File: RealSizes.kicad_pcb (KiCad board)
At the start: 2 copper layers, 104 parts

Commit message: Plots
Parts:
- removed the REF** at (143.3, 39.9)
- removed the REF** at (26.2, 20.1)
- removed the REF** at (228.6, 41.9)
- removed the REF** at (103.6, 127.0)
- removed the REF** at (139.2, 191.3)
- removed the REF** at (103.6, 114.3)
- added 01005_0402M: C_01005_0402Metric, Capacitor_SMD:C_01005_0402Metric, F.Cu at (264.5, 14.5)
- 5x1206: renamed from REF**; value R_Array_Convex_5x1206 -> 5x1206
- SMA-SMB: renamed from REF**; value D_SMA-SMB_Universal_Handsoldering -> SMA-SMB_Universal_Handsoldering
- TO-252-2 DPAK: renamed from REF**
- TO-263-2 DDPAK: renamed from REF**
- TO-5-8, TO-78-8, TO-99-8 : renamed from REF**
- moved 5x1206 239.6 mm to (262.5, 61.5), turned to 90 degrees
- moved 0402_1005M 238.5 mm to (264.5, 18.0)
- moved 0201_0603M 238.5 mm to (264.5, 16.0)
- moved 0805_2012M 238.0 mm to (264.0, 22.5)
- moved 2010_5025M 238.0 mm to (263.0, 38.5)
- moved 0603_1608M 237.9 mm to (264.0, 20.0)
- moved 2512_6332M 237.8 mm to (262.5, 43.0)
- moved 1210_3225M 237.8 mm to (263.5, 29.5)
- moved 2816_7142M 237.7 mm to (262.0, 48.5)
- moved 1206_3216M 237.6 mm to (263.5, 25.5)
- moved 1812_4532M 237.6 mm to (263.0, 34.0)
- moved 4020_10251M 236.8 mm to (260.5, 55.0)
- moved DSUB-9_P2.77x2.84mm 179.0 mm to (24.7, 114.7)
- moved DSUB-15-HD_P2.29x1.98mm 178.1 mm to (26.0, 131.2)
- moved DSUB-15_P2.77x2.84mm 173.4 mm to (24.5, 149.8)
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- renumbered REF** to 0201_0603M, REF** to 0402_1005M, REF** to 0603_1608M, REF** to 0805_2012M, REF** to 1206_3216M, REF** to 1210_3225M, REF** to 1812_4532M, REF** to 2010_5025M, REF** to 2512_6332M, REF** to 2816_7142M, REF** to 4020_10251M, REF** to BGA-25_6.35x6.35mm_5x5_P1.27mm, REF** to CPGA196, REF** to CSG324, REF** to DFN-6_1.3x1.2mm_P0.4mm, REF** to DFN-8_2x2mm_P0.5mm, REF** to DFN1006-3, REF** to DIP-14_W7.62mm_Socket, REF** to DIP-8_W7.62mm_Socket, REF** to DSUB-15-HD_P2.29x1.98mm, REF** to DSUB-15_P2.77x2.84mm, REF** to DSUB-25_P2.77x2.84mm, REF** to DSUB-37_P2.77x2.84mm, REF** to DSUB-9_P2.77x2.84mm, REF** to LED_D10.0mm, REF** to LED_D3.0mm, REF** to LED_D4.0mm, REF** to LED_D5.0mm, REF** to LED_D8.0mm, REF** to MSOP-16_3x4.039mm_P0.5mm, REF** to MSOP-8_3x3mm_P0.65mm, REF** to MiniMELF, REF** to QFN-16-1EP_5x5mm_P0.8mm_EP2.7x2.7mm, REF** to SC-59, REF** to SC-70-8, REF** to SC-82AA, REF** to SO-8, REF** to SOD-123, REF** to SOD-323, REF** to SOD-523, REF** to SOD-882, REF** to SOIC-16_3.9x9.9mm_P1.27mm, REF** to SOT-223, REF** to SOT-223-5, REF** to SOT-223-6, REF** to SOT-223-8, REF** to SOT-23, REF** to SOT-23-5, REF** to SOT-323_SC-70, REF** to SOT-353_SC-70-5, REF** to SOT-523, REF** to SOT-89-3, REF** to TO-220-3, REF** to TO-220-3_Vertical, REF** to TO-220-5_P3.4x3.7mm_StaggerEven_Lead3.8mm, REF** to TO-220-5_P3.4x3.8mm_StaggerEven_Lead7.13mm, REF** to TO-247-3, REF** to TO-263-5, REF** to TO-268-2, REF** to TO-277A, REF** to TO-3, REF** to TO-92, REF** to TO-92Flat, REF** to TO-92L_Inline, REF** to TP1.0x1.0, REF** to TP1.0x1.0_Drl_0.5, REF** to TP1.5x1.5, REF** to TP1.5x1.5_Drl_0.7, REF** to TP2.0x2.0_Drl_1.0, REF** to TP2x2, REF** to TP3.0x3.0_Drl_1.5, REF** to TP3x3, REF** to TPD1.0mm, REF** to TPD1.0mm_Drl_0.5mm, REF** to TPD1.5mm, REF** to TPD1.5mm_Drl_0.7mm, REF** to TPD2.0mm, REF** to TPD2.0mm_PTH, REF** to TPD3.0mm, REF** to TPD3.0mm_PTH, REF** to TSOT-23, REF** to TSOT-23-5, REF** to TSOT-23-6, REF** to TSOT-23-8, REF** to TSSOP-16_4.4x3.6mm_P0.4mm, REF** to TSSOP-8_3x3mm_P0.65mm, REF** to WSON6_1.5x1.5mm_P0.5mm
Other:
- board text removed: "DDPAK"
- board text removed: "DPAK"

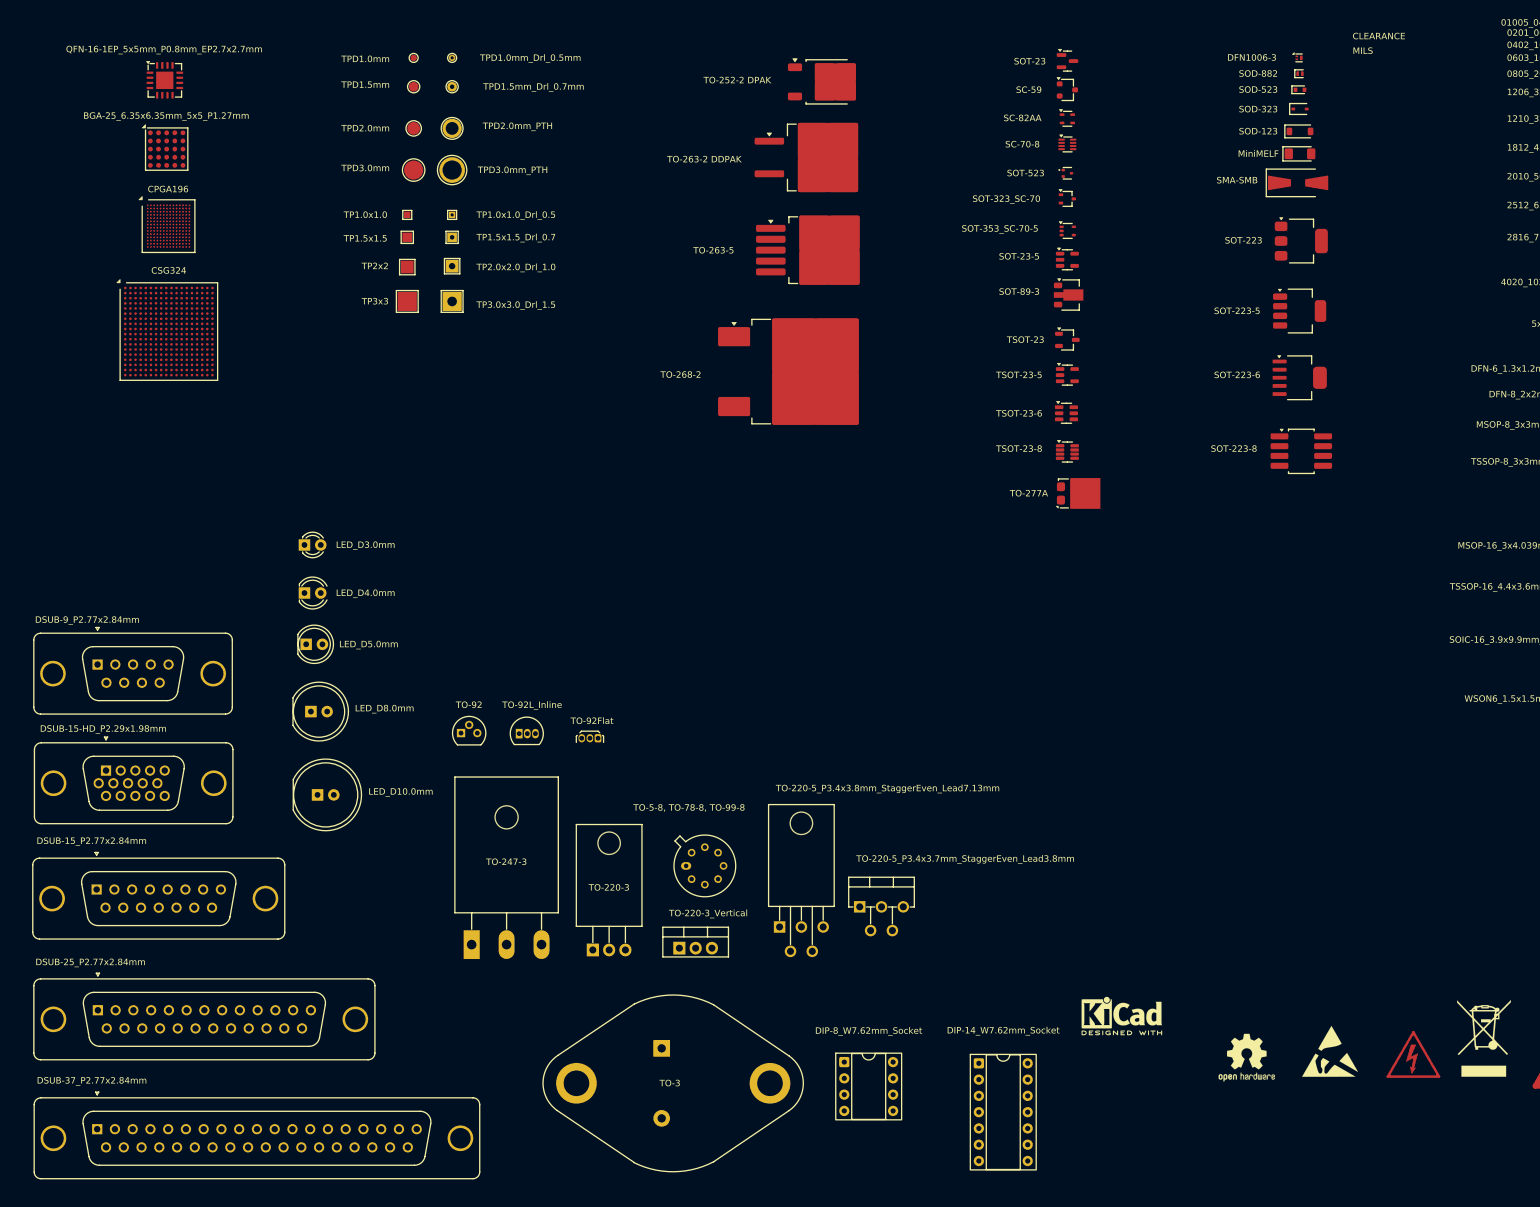
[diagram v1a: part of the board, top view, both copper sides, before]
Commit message: added diodes types
Need to ad diff, traces tracks c;learence
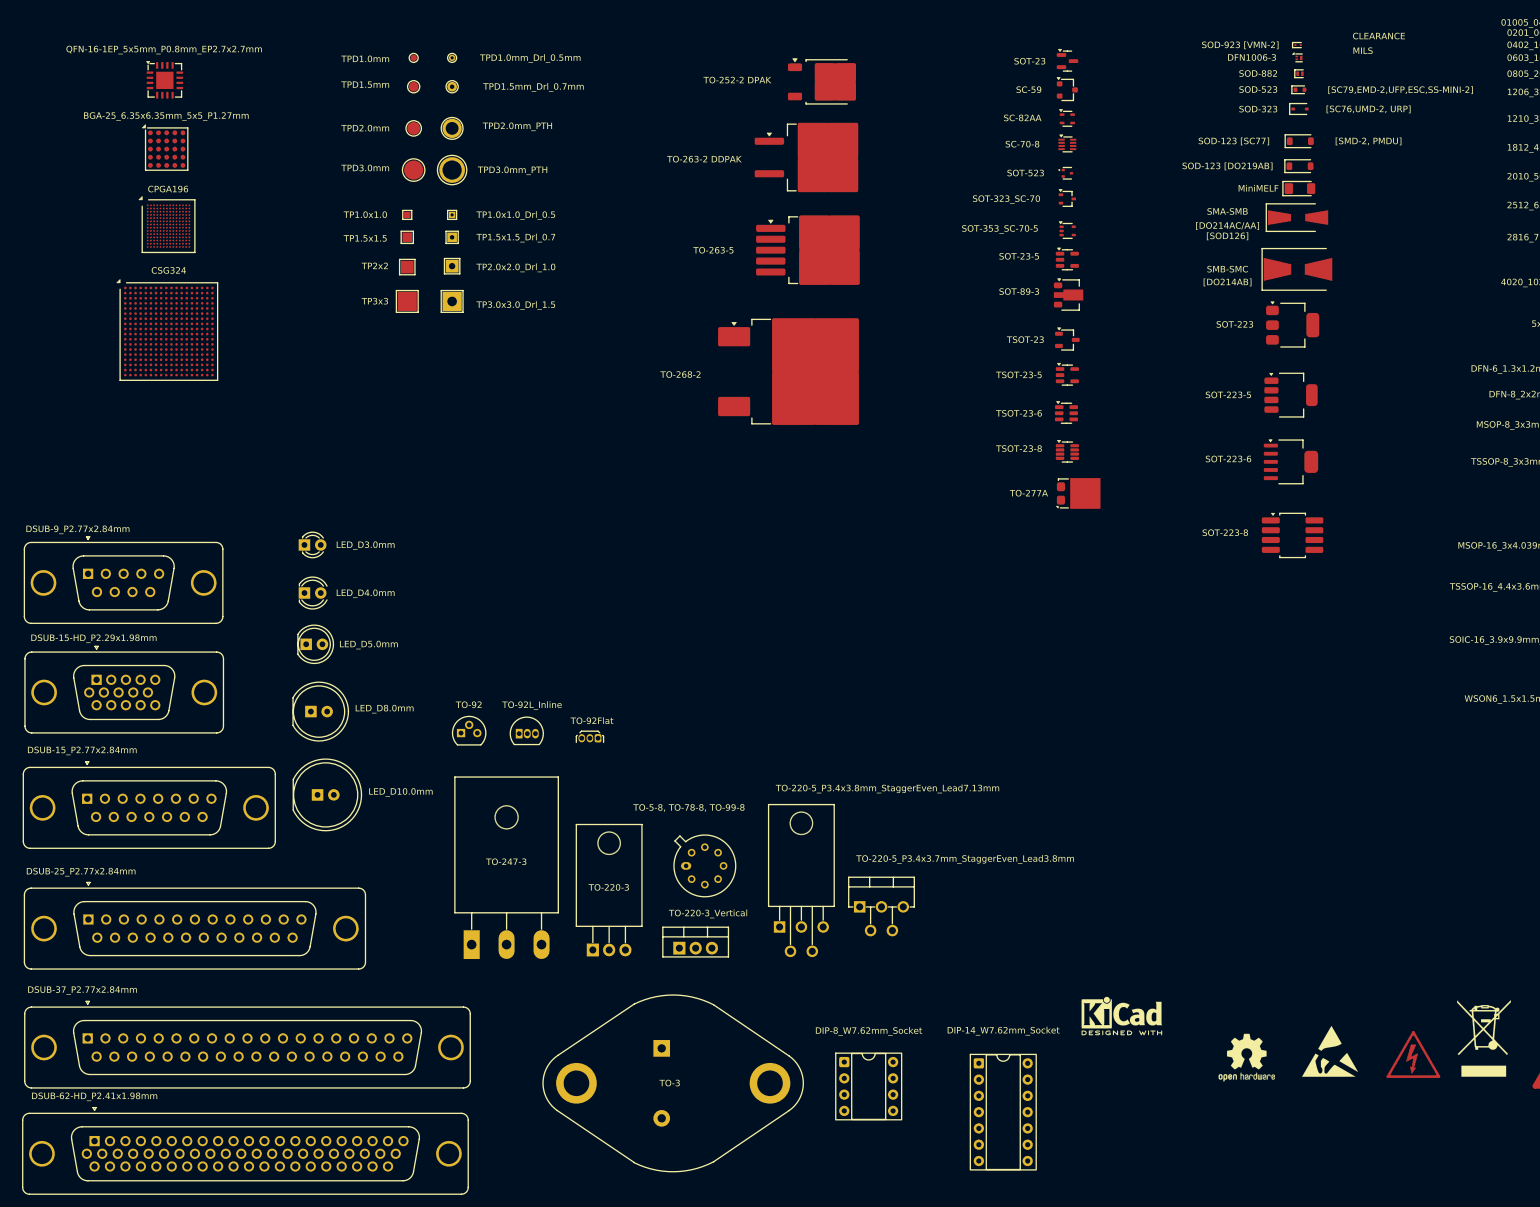
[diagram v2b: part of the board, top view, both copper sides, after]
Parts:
- added DSUB-62-HD_P2.41x1.98mm: DSUB-62-HD_Pins_Vertical_P2.41x1.98mm_MountingHoles, Connector_Dsub:DSUB-62-HD_Pins_Vertical_P2.41x1.98mm_MountingHoles, F.Cu at (24.2, 189.0)
- added SMB-SMC: D_SMB-SMC_Universal_Handsoldering, Diode_SMD:D_SMB-SMC_Universal_Handsoldering, F.Cu at (212.0, 53.0)
- added SOD-123 [SC77]: D_SOD-123, Diode_SMD:D_SOD-123, F.Cu at (212.3, 33.0)
- added SOD-923 [VMN-2]: D_SOD-923, Diode_SMD:D_SOD-923, F.Cu at (212.0, 18.0)
- SOD-123 [DO219AB]: renamed from SOD-123
- moved DSUB-15-HD_P2.29x1.98mm 14.2 mm to (24.5, 117.0)
- moved DSUB-15_P2.77x2.84mm 14.2 mm to (23.1, 135.6)
- moved DSUB-25_P2.77x2.84mm 14.2 mm to (23.2, 154.4)
- moved DSUB-37_P2.77x2.84mm 14.2 mm to (23.1, 173.0)
- moved DSUB-9_P2.77x2.84mm 14.2 mm to (23.2, 100.5)
- moved SOT-223-5 13.2 mm to (210.9, 72.6)
- moved SOT-223-6 13.2 mm to (210.9, 83.0)
- moved SOT-223 13.2 mm to (211.2, 61.7)
- moved SOT-223-8 13.2 mm to (211.2, 94.5)
- moved MiniMELF 5.42 mm to (212.3, 40.4)
- moved SMA-SMB 5.42 mm to (212.0, 44.9)
- moved SOD-123 [DO219AB] 5.42 mm to (212.3, 36.9)
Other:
- board text added: "[DO214AB]"
- board text added: "[DO214AC/AA] [SOD126]"
- board text added: "[SC76,UMD-2, URP]"
- board text added: "[SC79,EMD-2,UFP,ESC,SS-MINI-2]"
- board text added: "[SMD-2, PMDU]"

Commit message: added tracks , need to add diff
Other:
- board text added: "10 MILS"
- board text added: "12 MILS"
- board text added: "15 MILS"
- board text added: "18 MILS"
- board text added: "20 MILS"
- board text added: "3 MILS"
- board text added: "30 MILS"
- board text added: "40 MILS"
- board text added: "50 MILS"
- board text added: "6 MILS"
- board text added: "8 MILS"
- board text removed: "CLEARANCE"
- board text removed: "MILS"
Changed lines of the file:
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@@
+	)
+	(gr_line
+		(start 269.5 144)
+		(end 282.5 144)
+		(stroke
+			(width 0.1524)
+			(type solid)
+		)
+		(layer "F.SilkS")
 	)
 	(gr_line
@@
 	)
 	(gr_line
+		(start 269.5 150)
+		(end 282.5 150)
+		(stroke
+			(width 0.3048)
+			(type solid)
+		)
+		(layer "F.SilkS")
+	)
+	(gr_line
 		(start 283.5 90.5)
 		(end 279.5 90.5)
@@
 	)
 	(gr_line
+		(start 269.5 154)
+		(end 282.5 154)
+		(stroke
+			(width 0.4572)
+			(type solid)
+		)
+		(layer "F.SilkS")
+	)
+	(gr_line
 		(start 283.5 71.5)
 		(end 279.5 71.5)
@@
 	)
 	(gr_line
+		(start 269.5 148)
+		(end 282.5 148)
+		(stroke
+			(width 0.254)
+			(type solid)
+		)
+		(layer "F.SilkS")
+	)
+	(gr_line
 		(start 283.5 16.5)
 		(end 279.5 16.5)
@@
 	)
 	(gr_line
+		(start 269.5 152)
+		(end 282.5 152)
+		(stroke
+			(width 0.381)
+			(type solid)
+		)
+		(layer "F.SilkS")
+	)
+	(gr_line
 		(start 283.5 29.5)
 		(end 279.5 29.5)
@@
 	)
 	(gr_line
+		(start 269.5 160)
+		(end 282.5 160)
+		(stroke
+			(width 1.016)
+			(type solid)
+		)
+		(layer "F.SilkS")
+	)
+	(gr_line
 		(start 283.5 78.5)
 		(end 277.5 78.5)
@@
 	)
 	(gr_line
+		(start 269.5 156)
+		(end 282.5 156)
+		(stroke
+			(width 0.508)
+			(type solid)
+		)
+		(layer "F.SilkS")
+	)
+	(gr_line
+		(start 269.5 142)
+		(end 282.5 142)
+		(stroke
+			(width 0.0762)
+			(type solid)
+		)
+		(layer "F.SilkS")
+	)
+	(gr_line
 		(start 283.5 30.5)
 		(end 279.5 30.5)
@@
 	)
 	(gr_line
+		(start 269.5 158)
+		(end 282.5 158)
+		(stroke
+			(width 0.762)
+			(type solid)
+		)
+		(layer "F.SilkS")
+	)
+	(gr_line
 		(start 283.5 13.5)
 		(end 275.5 13.5)
@@
 	)
 	(gr_line
+		(start 269.5 146)
+		(end 282.5 146)
+		(stroke
+			(width 0.2032)
+			(type solid)
+		)
+		(layer "F.SilkS")
+	)
+	(gr_line
 		(start 283.5 62.5)
 		(end 279.5 62.5)
@@
 	)
 	(gr_line
+		(start 269.5 162)
+		(end 282.5 162)
+		(stroke
+			(width 1.27)
+			(type solid)
+		)
+		(layer "F.SilkS")
+	)
+	(gr_line
 		(start 283.5 65.5)
 		(end 279.5 65.5)
@@
 		)
 	)
+	(gr_text "20 MILS\n"
+		(at 259.5 156 0)
+		(layer "F.SilkS")
+		(effects
+			(font
+				(size 1 1)
+				(thickness 0.1)
+			)
+			(justify left bottom)
+		)
+	)
 	(gr_text "[SC79,EMD-2,UFP,ESC,SS-MINI-2]"
 		(at 228 25 0)
@@
 		)
 	)
+	(gr_text "30 MILS\n"
+		(at 259.5 158 0)
+		(layer "F.SilkS")
+		(effects
+			(font
+				(size 1 1)
+				(thickness 0.1)
+			)
+			(justify left bottom)
+		)
+	)
 	(gr_text "[SMD-2, PMDU]"
 		(at 223 33 0)
@@
 		)
 	)
-	(gr_text "MILS\n"
-		(at 220.5 19.5 0)
+	(gr_text "3 MILS\n"
+		(at 259.5 142 0)
+		(layer "F.SilkS")
+		(effects
+			(font
+				(size 1 1)
+				(thickness 0.1)
+			)
+			(justify left bottom)
+		)
+	)
+	(gr_text "10 MILS\n"
+		(at 259.5 148 0)
 		(layer "F.SilkS")
 		(effects
@@
 		)
 	)
+	(gr_text "6 MILS\n"
+		(at 259.5 144 0)
+		(layer "F.SilkS")
+		(effects
+			(font
+				(size 1 1)
+				(thickness 0.1)
+			)
+			(justify left bottom)
+		)
+	)
 	(gr_text "6"
 		(at 272.5 73.5 0)
@@
 		)
 	)
+	(gr_text "50 MILS\n"
+		(at 259.5 162 0)
+		(layer "F.SilkS")
+		(effects
+			(font
+				(size 1 1)
+				(thickness 0.1)
+			)
+			(justify left bottom)
+		)
+	)
 	(gr_text "[DO214AC/AA]\n[SOD126]"
 		(at 201 47 0)
@@
 		)
 	)
+	(gr_text "18 MILS\n"
+		(at 259.5 154 0)
+		(layer "F.SilkS")
+		(effects
+			(font
+				(size 1 1)
+				(thickness 0.1)
+			)
+			(justify left bottom)
+		)
+	)
+	(gr_text "12 MILS\n"
+		(at 259.5 150 0)
+		(layer "F.SilkS")
+		(effects
+			(font
+				(size 1 1)
+				(thickness 0.1)
+			)
+			(justify left bottom)
+		)
+	)
+	(gr_text "8 MILS\n"
+		(at 259.5 146 0)
+		(layer "F.SilkS")
+		(effects
+			(font
+				(size 1 1)
+				(thickness 0.1)
+			)
+			(justify left bottom)
+		)
+	)
 	(gr_text "[DO214AB]"
 		(at 201 55 0)
@@
 		)
 	)
+	(gr_text "40 MILS\n"
+		(at 259.5 160 0)
+		(layer "F.SilkS")
+		(effects
+			(font
+				(size 1 1)
+				(thickness 0.1)
+			)
+			(justify left bottom)
+		)
+	)
+	(gr_text "15 MILS\n"
+		(at 259.5 152 0)
+		(layer "F.SilkS")
+		(effects
+			(font
+				(size 1 1)
+				(thickness 0.1)
+			)
+			(justify left bottom)
+		)
+	)
 	(gr_text "10"
 		(at 272.5 113.5 0)
@@
 		(layer "F.SilkS")
 		(effects
-			(font
-				(size 1 1)
-				(thickness 0.1)
-			)
-			(justify left bottom)
-		)
-	)
-	(gr_text "CLEARANCE"
-		(at 220.5 17.214 0)
-		(layer "F.SilkS")
-		(effects

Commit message: REV1.2
Changes added From Rev1.1
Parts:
- added D2: SMAJ26A, SMAJ26A:DIOM5026X229N, F.Cu at (145.0, 82.0)
- added REF**: SOD-128, Diode_SMD:D_SOD-128, F.Cu at (212.0, 44.0)
- added REF**: USBC, Connector_USB:USB_C_Receptacle_G-Switch_GT-USB-7010ASV, F.Cu at (22.0, 88.0)
- added REF**: USB_Micro-B, Connector_USB:USB_Micro-B_Amphenol_10118194-0001LF_Horizontal, F.Cu at (35.0, 87.0)
- added SMBJ: 5436X261, SMBJ20A:DIOM5436X261N, F.Cu at (145.0, 88.0)
- added SMCJ: 7959X262, SMCJ48A:DIOM7959X262N, F.Cu at (145.0, 97.0)
- added SMDJ: 6859X262, SMDJ60CA:DIOM6859X262N, F.Cu at (145.0, 108.0)
- added SMFJ: TVS_SMF45A, SMF45A:TVS_SMF45A, F.Cu at (145.0, 77.0)
- added SOD-962: DSN0603_0.6x0.3mm_P0.4mm, Diode_SMD:Nexperia_DSN0603-2_0.6x0.3mm_P0.4mm, F.Cu at (212.0, 16.0)
- CPGA196 P0.5: renamed from CPGA196
- CSG324 P0.8: renamed from CSG324
- TO-268-2 D3PAK: renamed from TO-268-2
- moved TO-220-5_P3.4x3.8mm_StaggerEven_Lead7.13mm 43.3 mm to (170.1, 174.4), turned to 90 degrees
- moved TO-220-5_P3.4x3.7mm_StaggerEven_Lead3.8mm 20.4 mm to (138.9, 172.3)
- moved REF** 20.1 mm to (184.0, 174.0)
- moved TO-5-8, TO-78-8, TO-99-8  15.9 mm to (101.1, 150.0)
- moved DIP-14_W7.62mm_Socket 15.5 mm to (155.4, 190.8), turned to 90 degrees
- moved TO-220-3_Vertical 14.1 mm to (102.0, 163.0)
- moved TO-220-3 13.5 mm to (89.5, 164.2)
- moved REF** 12.1 mm to (195.9, 173.4)
- moved TO-247-3 11.1 mm to (72.5, 161.9)
- moved TO-263-2 DDPAK 8.00 mm to (142.7, 29.8)
- moved TO-263-5 7.47 mm to (142.9, 45.0)
- moved TO-268-2 D3PAK 7.47 mm to (139.5, 64.0)
- moved TO-252-2 DPAK 7.23 mm to (144.0, 19.0)
- moved DIP-8_W7.62mm_Socket 5.85 mm to (139.2, 182.2)
- moved SMA-SMB 5.08 mm to (212.0, 50.0)
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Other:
- board text added: "(Missing Footprints, Issues -> Request or Pull on Github)"
- board text added: "---------------------------------- SMD PACKAGES: METRIC IMPERIAL ---------------------------------- 2920 7.4 x 5.1 0.29 x 0.20 7451 2917 7.3 x 4.3 0.29 x 0.17 7343 2725 6.9 x 6.3 0.27 x 0.25 6863 2512 6.3 x 3.2 0.25 x 0.125 6332 2412 6.0 x 3.2 0.24 x 0.12 6032 2318 5.8 x 4.6 0.23 x 0.18 5864 2225 5.6 x 6.4 0.22 x 0.25 5664 2220 5.6 x 5.0 0.22 x 0.20 5650 2010 5.0 x 2.5 0.20 x 0.10 5025 1825 4.5 x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"
- board text added: "1.6mm"
- board text added: "100 MILS"
- board text added: "150 MILS"
- board text added: "2.05mm"
- board text added: "2.5mm"
- board text added: "3.3mm"
- board text added: "3U 100mm x 160mm"
- board text added: "4.2mm"
- board text added: "5mm"
- board text added: "6U 233.35mm x 160mm"
- board text added: "ARIEL FONT HEIGHT"
- board text added: "AWG Dia(mm) Area mm2 mR/m Amps ---------------------------- 14 1.628 2.08 8.286 15 15 1.45 1.65 10.45 15 16 1.291 1.31 13.17 12 17 1.15 1.04 16.61 12 18 1.024 0.823 20.95 10 19 0.912 0.653 26.42 10 20 0.812 0.518 33.31 5 21 0.723 0.41 42 5 22 0.644 0.326 52.96 3 23 0.573 0.258 66.79 3 24 0.511 0.205 84.22 2.1 25 0.455 0.162 106.2 2.1 26 0.405 0.129 133.9 1.3 ---------------------------"
- board text added: "Drill Size"
- board text added: "M2"
- board text added: "M2.5"
- board text added: "M3"
- board text added: "M4"
- board text added: "M5"
- board text added: "M6"
- board text added: "SMAJ"
- board text added: "TO-5-8 TO-78-8 TO-99-8"
- board text added: "W0.5H0.5 ARIEL"
- board text added: "W1.5H1.5 ARIEL"
- board text added: "W1H1 ARIEL"
- board text added: "W2.5H2.5 ARIEL"
- board text added: "W2H2 ARIEL"
- board text added: "W3.5H3.5 ARIEL"
- board text added: "W3H3 ARIEL"
- board text added: "W4.5H4.5 ARIEL"
- board text added: "W4H4 ARIEL"
- board text added: "W5H5 ARIEL"
- board text added: "https://github.com/Arvind595/Common-Footprints-Stencil-A4"

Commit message: REV1.21
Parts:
- added 1/2W: R_Axial_DIN0309_L9.0mm_D3.2mm_P15.24mm_Horizontal, Resistor_THT:R_Axial_DIN0309_L9.0mm_D3.2mm_P15.24mm_Horizontal, F.Cu at (166.0, 102.0)
- added 1/4W: R_Axial_DIN0207_L6.3mm_D2.5mm_P10.16mm_Horizontal, Resistor_THT:R_Axial_DIN0207_L6.3mm_D2.5mm_P10.16mm_Horizontal, F.Cu at (168.0, 97.0)
- added 1W: R_Axial_DIN0411_L9.9mm_D3.6mm_P15.24mm_Horizontal, Resistor_THT:R_Axial_DIN0411_L9.9mm_D3.6mm_P15.24mm_Horizontal, F.Cu at (166.0, 108.0)
- added 5W: R_Axial_DIN0922_L20.0mm_D9.0mm_P30.48mm_Horizontal, Resistor_THT:R_Axial_DIN0922_L20.0mm_D9.0mm_P30.48mm_Horizontal, F.Cu at (157.0, 117.0)
- added REF**: SOT-723, Package_TO_SOT_SMD:SOT-723, F.Cu at (176.0, 16.0)
- added REF**: SOT-143, Package_TO_SOT_SMD:SOT-143, F.Cu at (184.0, 64.0)
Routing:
- net (no net): vias 0 -> 4
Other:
- board text added: "D0.6mm H0.3mm"
- board text added: "D1mm H0.5mm"
- board text added: "D2mm H1mm"
- board text added: "D3.5mm H2.5mm"
- board text added: "Vias"
